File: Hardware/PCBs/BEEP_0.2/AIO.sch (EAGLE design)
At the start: 88 parts, among them IC1 74HC238SSOP, IC2 74HC238SSOP, IC3 ULN2803ASOP18, IC4 ULN2803ASOP18, IC5 ATXMEGA64D3-AU, IC6 GY-81, IC7 TB6612FNG, IC8 TS34119SMD, IC9 RASPBERRY-PI, Q1 DMN2075U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

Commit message: add connections from xmega to encoders enhance Borders
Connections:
- net ENCODER_L1: now also IC5.PC4
- net ENCODER_L2: now also IC5.PC5
- net ENCODER_R1: now also IC5.PC6
- net ENCODER_R2: now also IC5.PC7
- net MOTOR_STBY: now also IC5.PA6; no longer IC5.PC6
- net POWER_OFF: now also IC5.PA7; no longer IC5.PC7
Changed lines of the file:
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@@
 </segment>
 <segment>
-<wire x1="129.54" y1="99.06" x2="134.62" y2="99.06" width="0.1524" layer="91"/>
-<label x="134.62" y="99.06" size="1.27" layer="95" xref="yes"/>
-<pinref part="IC5" gate="G$1" pin="PC6"/>
+<label x="139.7" y="144.78" size="1.27" layer="95" xref="yes"/>
+<wire x1="129.54" y1="144.78" x2="139.7" y2="144.78" width="0.1524" layer="91"/>
+<pinref part="IC5" gate="G$1" pin="PA6"/>
 </segment>
 </net>
@@
 <label x="467.36" y="81.28" size="1.27" layer="95" xref="yes"/>
 </segment>
+<segment>
+<pinref part="IC5" gate="G$1" pin="PC4"/>
+<wire x1="129.54" y1="104.14" x2="134.62" y2="104.14" width="0.1524" layer="91"/>
+<label x="134.62" y="104.14" size="1.27" layer="95" xref="yes"/>
+</segment>
 </net>
 <net name="N$23" class="0">
@@
 <label x="515.62" y="83.82" size="1.27" layer="95" xref="yes"/>
 </segment>
+<segment>
+<pinref part="IC5" gate="G$1" pin="PC5"/>
+<wire x1="129.54" y1="101.6" x2="134.62" y2="101.6" width="0.1524" layer="91"/>
+<label x="134.62" y="101.6" size="1.27" layer="95" xref="yes"/>
+</segment>
 </net>
 <net name="ENCODER_R1" class="0">
@@
 <label x="467.36" y="142.24" size="1.27" layer="95" xref="yes"/>
 </segment>
+<segment>
+<pinref part="IC5" gate="G$1" pin="PC6"/>
+<wire x1="129.54" y1="99.06" x2="134.62" y2="99.06" width="0.1524" layer="91"/>
+<label x="134.62" y="99.06" size="1.27" layer="95" xref="yes"/>
+</segment>
 </net>
 <net name="ENCODER_R2" class="0">
@@
 <junction x="505.46" y="144.78"/>
 <label x="515.62" y="144.78" size="1.27" layer="95" xref="yes"/>
+</segment>
+<segment>
+<pinref part="IC5" gate="G$1" pin="PC7"/>
+<wire x1="129.54" y1="96.52" x2="134.62" y2="96.52" width="0.1524" layer="91"/>
+<label x="134.62" y="96.52" size="1.27" layer="95" xref="yes"/>
 </segment>
 </net>
@@
 </segment>
 <segment>
-<pinref part="IC5" gate="G$1" pin="PC7"/>
-<wire x1="129.54" y1="96.52" x2="134.62" y2="96.52" width="0.1524" layer="91"/>
-<label x="134.62" y="96.52" size="1.27" layer="95" xref="yes"/>
-</segment>
-</net>
+<label x="139.7" y="142.24" size="1.27" layer="95" xref="yes"/>
+<wire x1="129.54" y1="142.24" x2="139.7" y2="142.24" width="0.1524" layer="91"/>
+<pinref part="IC5" gate="G$1" pin="PA7"/>
+</segment>
+</net>

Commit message: last? minor changes.
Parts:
- C13, C14: value (none) -> 10uF
- X11: value (none) -> line follow
- X12: value (none) -> motor
- X13: value (none) -> audio
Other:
- moved on the sheet: C13, C14
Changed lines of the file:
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@@
 <part name="X3" library="con-ftop-orientation-hole" deviceset="FTOP-8" device="" value="Sens0"/>
 <part name="X8" library="con-ftop-orientation-hole" deviceset="FTOP-8" device="" value="Sens4"/>
-<part name="X13" library="con-ftop-orientation-hole" deviceset="FTOP-4" device=""/>
-<part name="X12" library="con-ftop-orientation-hole" deviceset="FTOP-4" device=""/>
-<part name="X11" library="con-ftop-orientation-hole" deviceset="FTOP-10" device=""/>
-<part name="C13" library="rcl" deviceset="CPOL-EU" device="E2-5"/>
-<part name="C14" library="rcl" deviceset="CPOL-EU" device="E2-5"/>
+<part name="X13" library="con-ftop-orientation-hole" deviceset="FTOP-4" device="" value="audio"/>
+<part name="X12" library="con-ftop-orientation-hole" deviceset="FTOP-4" device="" value="motor"/>
+<part name="X11" library="con-ftop-orientation-hole" deviceset="FTOP-10" device="" value="line follow"/>
+<part name="C13" library="rcl" deviceset="CPOL-EU" device="E2-5" value="10uF"/>
+<part name="C14" library="rcl" deviceset="CPOL-EU" device="E2-5" value="10uF"/>
 </parts>
 <sheets>
@@
 <instance part="X11" gate="-9" x="243.84" y="129.54" rot="MR180"/>
 <instance part="X11" gate="-10" x="243.84" y="132.08" rot="MR180"/>
-<instance part="C13" gate="G$1" x="411.48" y="144.78"/>
-<instance part="C14" gate="G$1" x="406.4" y="162.56"/>
+<instance part="C13" gate="G$1" x="406.4" y="144.78"/>
+<instance part="C14" gate="G$1" x="403.86" y="162.56"/>
 </instances>
 <busses>
@@
 <wire x1="401.32" y1="160.02" x2="401.32" y2="157.48" width="0.1524" layer="91"/>
 <pinref part="C15" gate="G$1" pin="1"/>
-<wire x1="401.32" y1="157.48" x2="406.4" y2="157.48" width="0.1524" layer="91"/>
+<wire x1="401.32" y1="157.48" x2="403.86" y2="157.48" width="0.1524" layer="91"/>
 <pinref part="GND20" gate="1" pin="GND"/>
-<wire x1="406.4" y1="157.48" x2="416.56" y2="157.48" width="0.1524" layer="91"/>
+<wire x1="403.86" y1="157.48" x2="416.56" y2="157.48" width="0.1524" layer="91"/>
 <wire x1="416.56" y1="154.94" x2="416.56" y2="157.48" width="0.1524" layer="91"/>
 <junction x="416.56" y="157.48"/>
 <pinref part="C14" gate="G$1" pin="-"/>
-<junction x="406.4" y="157.48"/>
+<junction x="403.86" y="157.48"/>
 </segment>
 <segment>
@@
 <wire x1="421.64" y1="139.7" x2="416.56" y2="139.7" width="0.1524" layer="91"/>
 <pinref part="GND18" gate="1" pin="GND"/>
-<wire x1="416.56" y1="139.7" x2="411.48" y2="139.7" width="0.1524" layer="91"/>
+<wire x1="416.56" y1="139.7" x2="406.4" y2="139.7" width="0.1524" layer="91"/>
 <wire x1="416.56" y1="134.62" x2="416.56" y2="139.7" width="0.1524" layer="91"/>
 <junction x="416.56" y="139.7"/>
@@
 <pinref part="C15" gate="G$1" pin="2"/>
 <pinref part="IC7" gate="G$1" pin="VCC"/>
-<wire x1="416.56" y1="165.1" x2="406.4" y2="165.1" width="0.1524" layer="91"/>
-<wire x1="406.4" y1="165.1" x2="381" y2="165.1" width="0.1524" layer="91"/>
+<wire x1="416.56" y1="165.1" x2="403.86" y2="165.1" width="0.1524" layer="91"/>
+<wire x1="403.86" y1="165.1" x2="381" y2="165.1" width="0.1524" layer="91"/>
 <wire x1="416.56" y1="165.1" x2="416.56" y2="172.72" width="0.1524" layer="91"/>
 <junction x="416.56" y="165.1"/>
 <pinref part="+3V9" gate="G$1" pin="+3V3"/>
 <pinref part="C14" gate="G$1" pin="+"/>
-<junction x="406.4" y="165.1"/>
+<junction x="403.86" y="165.1"/>
 </segment>
 <segment>
@@
 <junction x="381" y="147.32"/>
 <pinref part="SUPPLY1" gate="G$1" pin="+7V"/>
-<wire x1="381" y1="147.32" x2="411.48" y2="147.32" width="0.1524" layer="91"/>
-<wire x1="411.48" y1="147.32" x2="421.64" y2="147.32" width="0.1524" layer="91"/>
+<wire x1="381" y1="147.32" x2="406.4" y2="147.32" width="0.1524" layer="91"/>
 <wire x1="421.64" y1="147.32" x2="421.64" y2="177.8" width="0.1524" layer="91"/>
 <pinref part="IC7" gate="G$1" pin="VM1"/>
@@
 <junction x="421.64" y="147.32"/>
 <pinref part="C16" gate="G$1" pin="2"/>
-<wire x1="421.64" y1="147.32" x2="411.48" y2="147.32" width="0.1524" layer="91"/>
+<wire x1="421.64" y1="147.32" x2="406.4" y2="147.32" width="0.1524" layer="91"/>
 <junction x="421.64" y="147.32"/>
 <pinref part="C13" gate="G$1" pin="+"/>
-<junction x="411.48" y="147.32"/>
-</segment>
-<segment>
+<junction x="406.4" y="147.32"/>
+</segment>
+<segment>

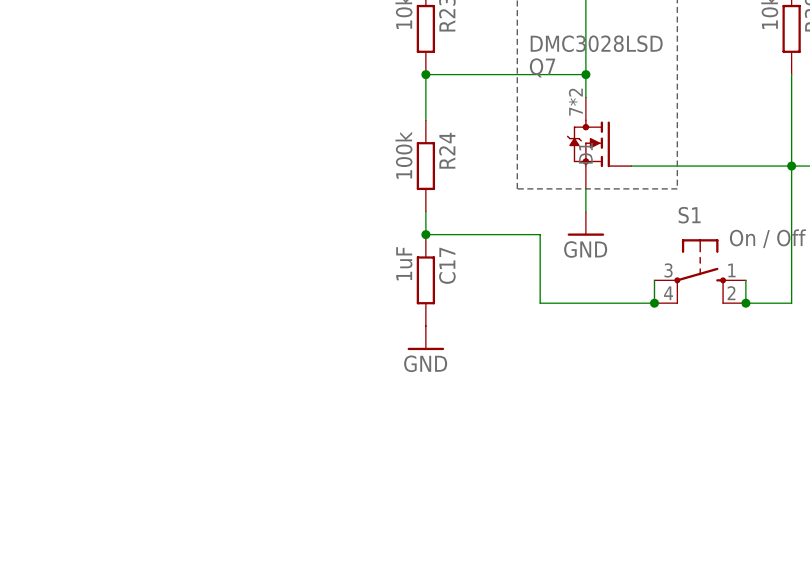
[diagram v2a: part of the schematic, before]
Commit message: change value of cap in of off circuit continue case design
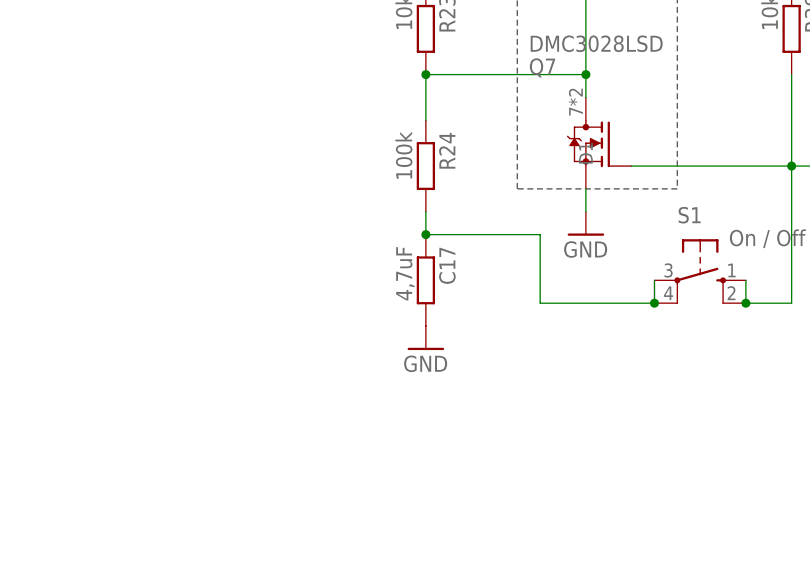
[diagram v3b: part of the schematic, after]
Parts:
- C17: value 1uF -> 4,7uF
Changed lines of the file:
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@@
 <part name="R24" library="resistor" deviceset="R-EU_" device="M0805" value="100k"/>
 <part name="R30" library="resistor" deviceset="R-EU_" device="M0805" value="10k"/>
-<part name="C17" library="resistor" deviceset="R-EU_" device="M0805" value="1uF"/>
+<part name="C17" library="resistor" deviceset="R-EU_" device="M0805" value="4,7uF"/>
 <part name="GND41" library="supply1" deviceset="GND" device=""/>
 <part name="GND42" library="supply1" deviceset="GND" device=""/>
